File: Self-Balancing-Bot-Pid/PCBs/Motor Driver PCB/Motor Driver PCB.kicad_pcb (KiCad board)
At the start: 2 copper layers, 2 parts, among them IC1 AS5600-ASOT, U1 A4988SETTR-T

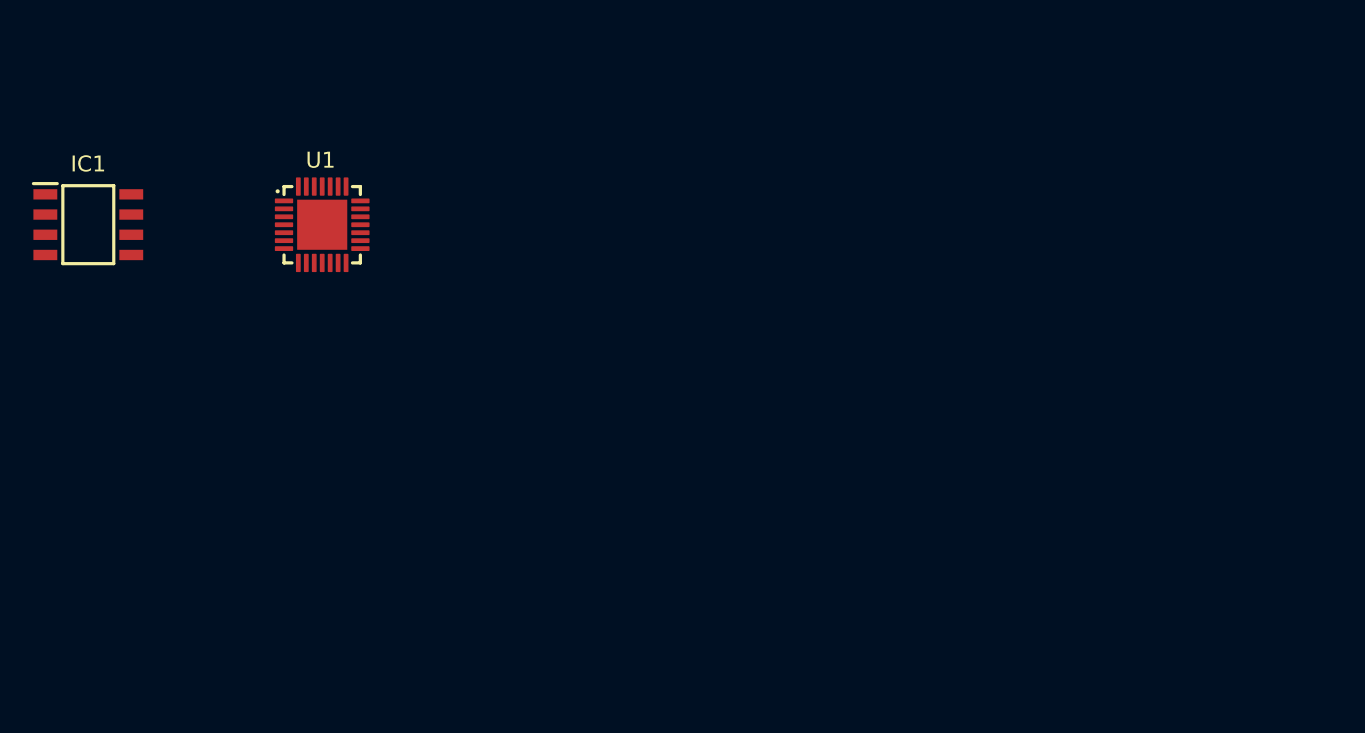
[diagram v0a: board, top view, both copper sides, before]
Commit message: Updated gitignore to ignore certain Kicad files. Ran ERC and DRC in Kicad, fixed any remaining issues, and now ready to route.
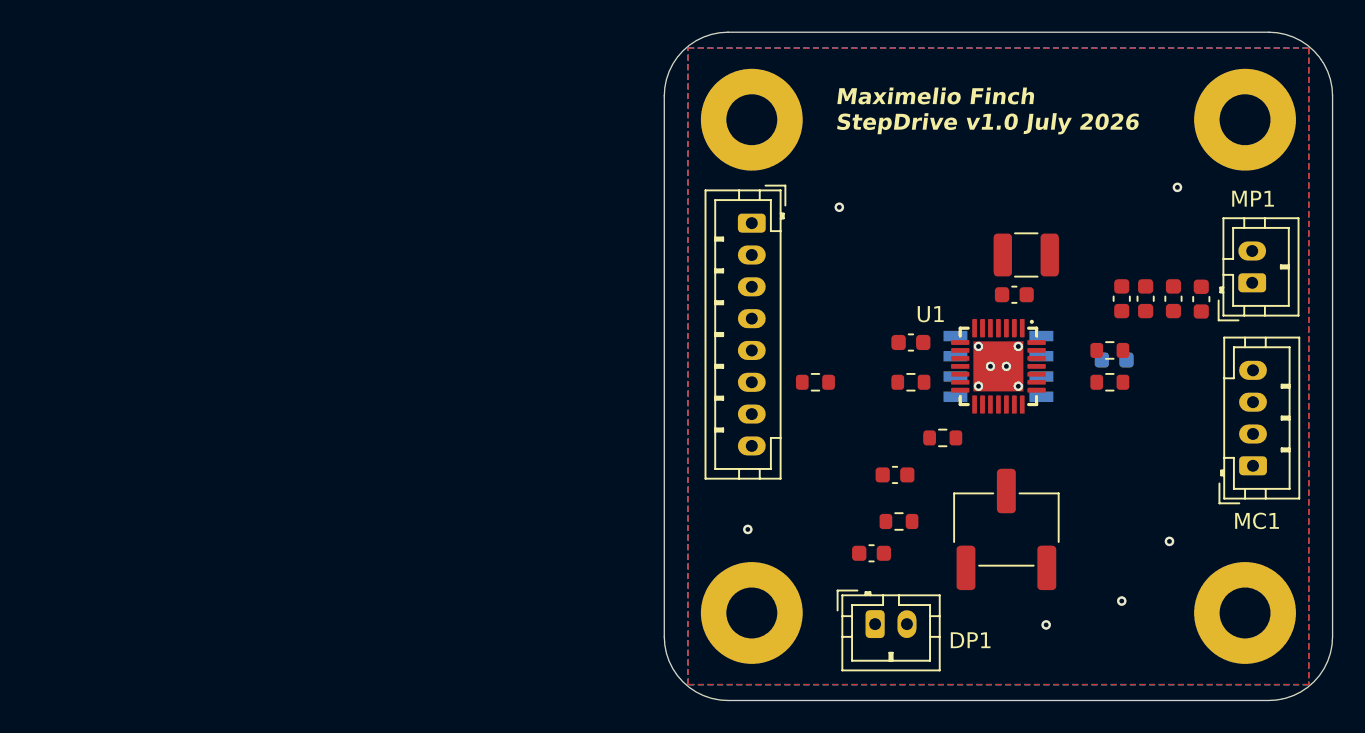
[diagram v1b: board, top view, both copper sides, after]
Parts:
- added C1: 0.1uF, Capacitor_SMD:C_0603_1608Metric, F.Cu at (185.0, 97.5)
- added C10: 100uF, Capacitor_SMD:C_0603_1608Metric, F.Cu at (191.8, 97.8)
- added C2: 4.7uF, Capacitor_SMD:C_0603_1608Metric, F.Cu at (196.8, 97.8)
- added C3: 0.1uF, Capacitor_SMD:C_0603_1608Metric, F.Cu at (195.0, 97.8)
- added C4: 0.22uF, Capacitor_SMD:C_0603_1608Metric, F.Cu at (176.0, 113.8)
- added C5: 0.1uF, Capacitor_SMD:C_0603_1608Metric, F.Cu at (193.2, 97.8)
- added C6: 0.1uF, Capacitor_SMD:C_1210_3225Metric, F.Cu at (185.8, 95.0)
- added C7: 0.22uF, Capacitor_SMD:C_0603_1608Metric, F.Cu at (178.5, 100.5)
- added C8: 0.1uF, Capacitor_SMD:C_0603_1608Metric, F.Cu at (177.5, 108.8)
- added C9: 0.1uF, Capacitor_SMD:C_0603_1608Metric, B.Cu at (191.3, 101.6)
- added DP1: Conn_01x02_Pin, Connector_JST:JST_PH_B2B-PH-K_1x02_P2.00mm_Vertical, F.Cu at (176.2, 118.2)
- added Hole1: MountingHole_3.2mm_M3_Pad, MountingHole:MountingHole_3.2mm_M3_Pad, F.Cu at (168.5, 86.5)
- added Hole2: MountingHole_3.2mm_M3_Pad, MountingHole:MountingHole_3.2mm_M3_Pad, F.Cu at (168.5, 117.5)
- added Hole3: MountingHole_3.2mm_M3_Pad, MountingHole:MountingHole_3.2mm_M3_Pad, F.Cu at (199.5, 86.5)
- added Hole4: MountingHole_3.2mm_M3_Pad, MountingHole:MountingHole_3.2mm_M3_Pad, F.Cu at (199.5, 117.5)
- added J1: Conn_01x08_Pin, Connector_JST:JST_PH_B8B-PH-K_1x08_P2.00mm_Vertical, F.Cu at (168.5, 93.0)
- added MC1: Conn_01x04_Pin, Connector_JST:JST_PH_B4B-PH-K_1x04_P2.00mm_Vertical, F.Cu at (200.0, 108.2)
- added MP1: Conn_01x02_Pin, Connector_JST:JST_PH_B2B-PH-K_1x02_P2.00mm_Vertical, F.Cu at (199.9, 96.8)
- added R1: 100k, Resistor_SMD:R_0603_1608Metric, F.Cu at (180.5, 106.5)
- added R3: 10k, Resistor_SMD:R_0603_1608Metric, F.Cu at (178.5, 103.0)
- added R4: 0.05, Resistor_SMD:R_0603_1608Metric, F.Cu at (191.0, 101.0)
- added R5: 0.05, Resistor_SMD:R_0603_1608Metric, F.Cu at (191.0, 103.0)
- added R6: 20k, Resistor_SMD:R_0603_1608Metric, F.Cu at (177.8, 111.8)
- added R7: 100k, Resistor_SMD:R_0603_1608Metric, F.Cu at (172.5, 103.0)
- added RV1: 10k, Potentiometer_SMD:Potentiometer_Bourns_3269W_Vertical, F.Cu at (184.5, 112.2)
- IC1: moved to B.Cu
- moved IC1 57.9 mm to (184.0, 102.0), turned to 180 degrees
- moved U1 43.4 mm to (184.0, 102.0), turned to -90 degrees
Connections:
- IC1 pad 2: unconnected-(IC1-VDD3V3-Pad2) -> VDD
- IC1 pad 3: unconnected-(IC1-OUT-Pad3) -> /OUT
- IC1 pad 4: unconnected-(IC1-GND-Pad4) -> GND
- IC1 pad 5: unconnected-(IC1-PGO-Pad5) -> VDD
- IC1 pad 8: unconnected-(IC1-DIR-Pad8) -> /DIR
- U1 pad 1: unconnected-(U1-OUT2B-Pad1) -> Net-(MC1-Pin_1)
- U1 pad 10: unconnected-(U1-MS2-Pad10) -> Net-(J1-Pin_3)
- U1 pad 11: unconnected-(U1-MS3-Pad11) -> Net-(J1-Pin_4)
- U1 pad 12: unconnected-(U1-~{RESET}-Pad12) -> Net-(U1-~{RESET})
- U1 pad 13: unconnected-(U1-ROSC-Pad13) -> Net-(U1-ROSC)
- U1 pad 14: unconnected-(U1-~{SLEEP}-Pad14) -> Net-(U1-~{RESET})
- U1 pad 15: unconnected-(U1-VDD-Pad15) -> VDD
- U1 pad 16: unconnected-(U1-STEP-Pad16) -> Net-(J1-Pin_1)
- U1 pad 17: unconnected-(U1-REF-Pad17) -> Net-(U1-REF)
- U1 pad 18: unconnected-(U1-GND2-Pad18) -> GND
- U1 pad 19: unconnected-(U1-DIR-Pad19) -> Net-(J1-Pin_5)
- U1 pad 2: unconnected-(U1-~{ENABLE}-Pad2) -> Net-(J1-Pin_6)
- U1 pad 21: unconnected-(U1-OUT1B-Pad21) -> Net-(MC1-Pin_2)
- U1 pad 22: unconnected-(U1-VBB1-Pad22) -> +12V
- U1 pad 23: unconnected-(U1-SENSE1-Pad23) -> Net-(U1-SENSE1)
- U1 pad 24: unconnected-(U1-OUT1A-Pad24) -> Net-(MC1-Pin_4)
- U1 pad 26: unconnected-(U1-OUT2A-Pad26) -> Net-(MC1-Pin_3)
- U1 pad 27: unconnected-(U1-SENSE2-Pad27) -> Net-(U1-SENSE2)
- U1 pad 28: unconnected-(U1-VBB2-Pad28) -> +12V
- U1 pad 29: unconnected-(U1-PAD-Pad29) -> GND
- U1 pad 3: unconnected-(U1-GND1-Pad3) -> GND
- U1 pad 4: unconnected-(U1-CP1-Pad4) -> Net-(U1-CP1)
- U1 pad 5: unconnected-(U1-CP2-Pad5) -> Net-(U1-CP2)
- U1 pad 6: unconnected-(U1-VCP-Pad6) -> Net-(U1-VCP)
- U1 pad 8: unconnected-(U1-VREG-Pad8) -> Net-(U1-VREG)
- U1 pad 9: unconnected-(U1-MS1-Pad9) -> Net-(J1-Pin_2)
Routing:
- net GND: vias 0 -> 12
- added copper zone on B.Cu, net GND
- added copper zone on F.Cu, net GND
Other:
- board outline added: 42 x 42 mm
- board text added: "Maximelio Finch StepDrive v1.0 July 2026"

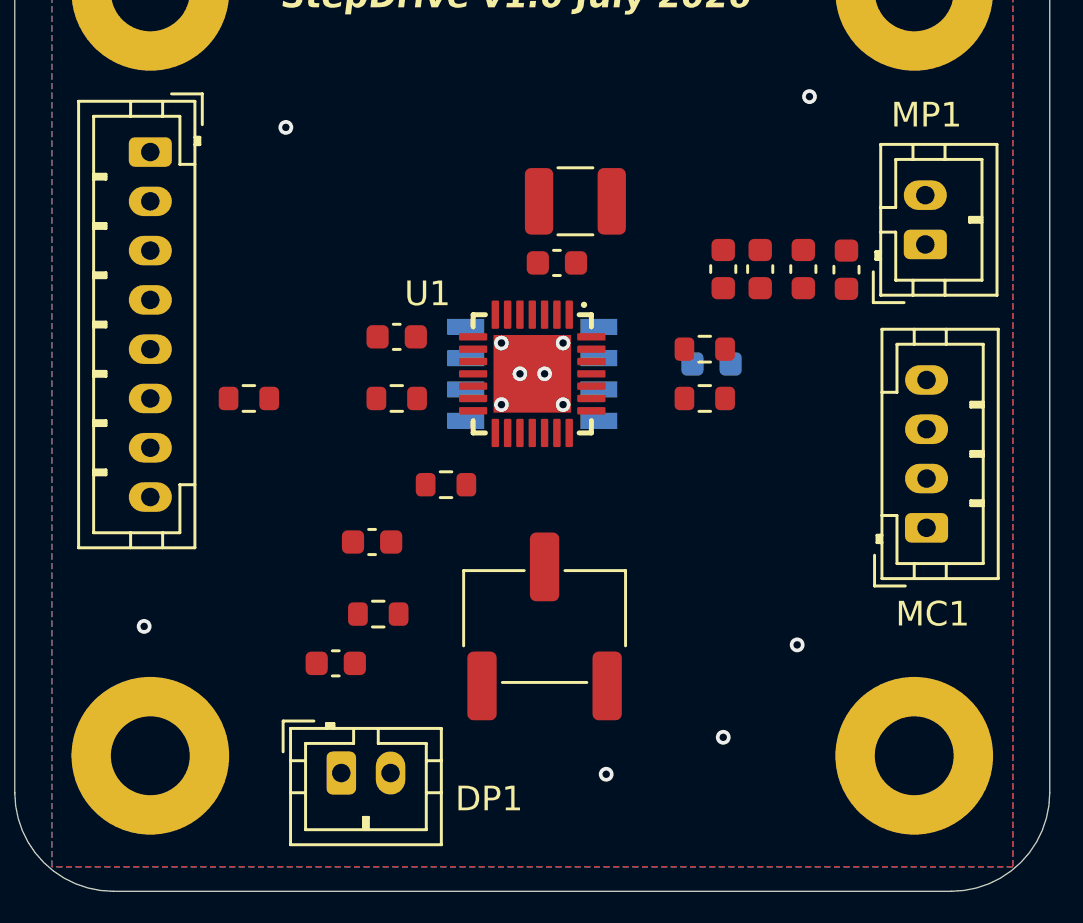
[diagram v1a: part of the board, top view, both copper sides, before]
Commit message: Finished initial routing of all traces
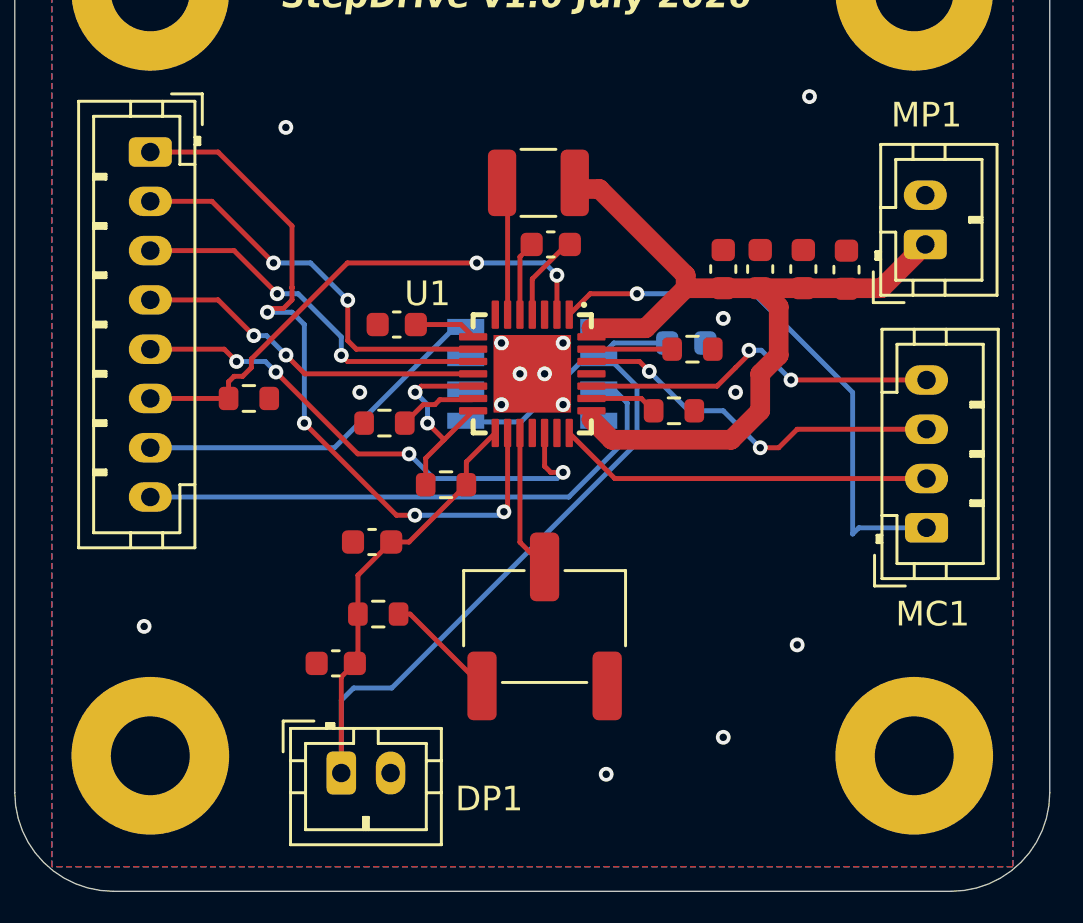
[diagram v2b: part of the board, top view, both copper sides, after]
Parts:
- moved C6 1.68 mm to (184.2, 94.2)
- moved R5 1.35 mm to (189.8, 103.5)
- moved C9 1.33 mm to (190.2, 100.8)
- moved R3 1.12 mm to (178.0, 104.0)
- moved C1 0.79 mm to (184.8, 96.8)
- moved C7 0.50 mm to (178.5, 100.0)
- moved R4 0.50 mm to (190.5, 101.0)
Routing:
- net VDD: track 0.00 -> 49.9 mm
- net +12V: track 0.00 -> 34.7 mm
- net Net-(J1-Pin_1): track 0.00 -> 29.9 mm, vias 0 -> 4
- net /OUT: track 0.00 -> 23.2 mm
- net Net-(MC1-Pin_1): track 0.00 -> 22.4 mm, vias 0 -> 1
- net Net-(J1-Pin_6): track 0.00 -> 21.3 mm, vias 0 -> 2
- net Net-(J1-Pin_5): track 0.00 -> 21.2 mm, vias 0 -> 4
- net Net-(J1-Pin_2): track 0.00 -> 16.5 mm, vias 0 -> 2
- net Net-(J1-Pin_3): track 0.00 -> 15.4 mm, vias 0 -> 2
- net Net-(MC1-Pin_3): track 0.00 -> 15.4 mm, vias 0 -> 2
- net Net-(MC1-Pin_2): track 0.00 -> 15.3 mm
- net Net-(MC1-Pin_4): track 0.00 -> 15.2 mm, vias 0 -> 2
- net /DIR: track 0.00 -> 14.8 mm
- net Net-(J1-Pin_4): track 0.00 -> 14.3 mm, vias 0 -> 2
- net Net-(U1-~{RESET}): track 0.00 -> 8.67 mm, vias 0 -> 2
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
